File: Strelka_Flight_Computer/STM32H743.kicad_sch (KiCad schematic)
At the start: 40 parts, among them J3 Conn_01x07, Q3 AO3400A, Q4 AO3400A, Q5 AO3401A, SW2 TS-1185-C-A-A-A, SW3 TS-1185-C-A-A-A, U6 STM32H743VITx, Y1 Q13FC1350000400, Y2 X1E0000210834

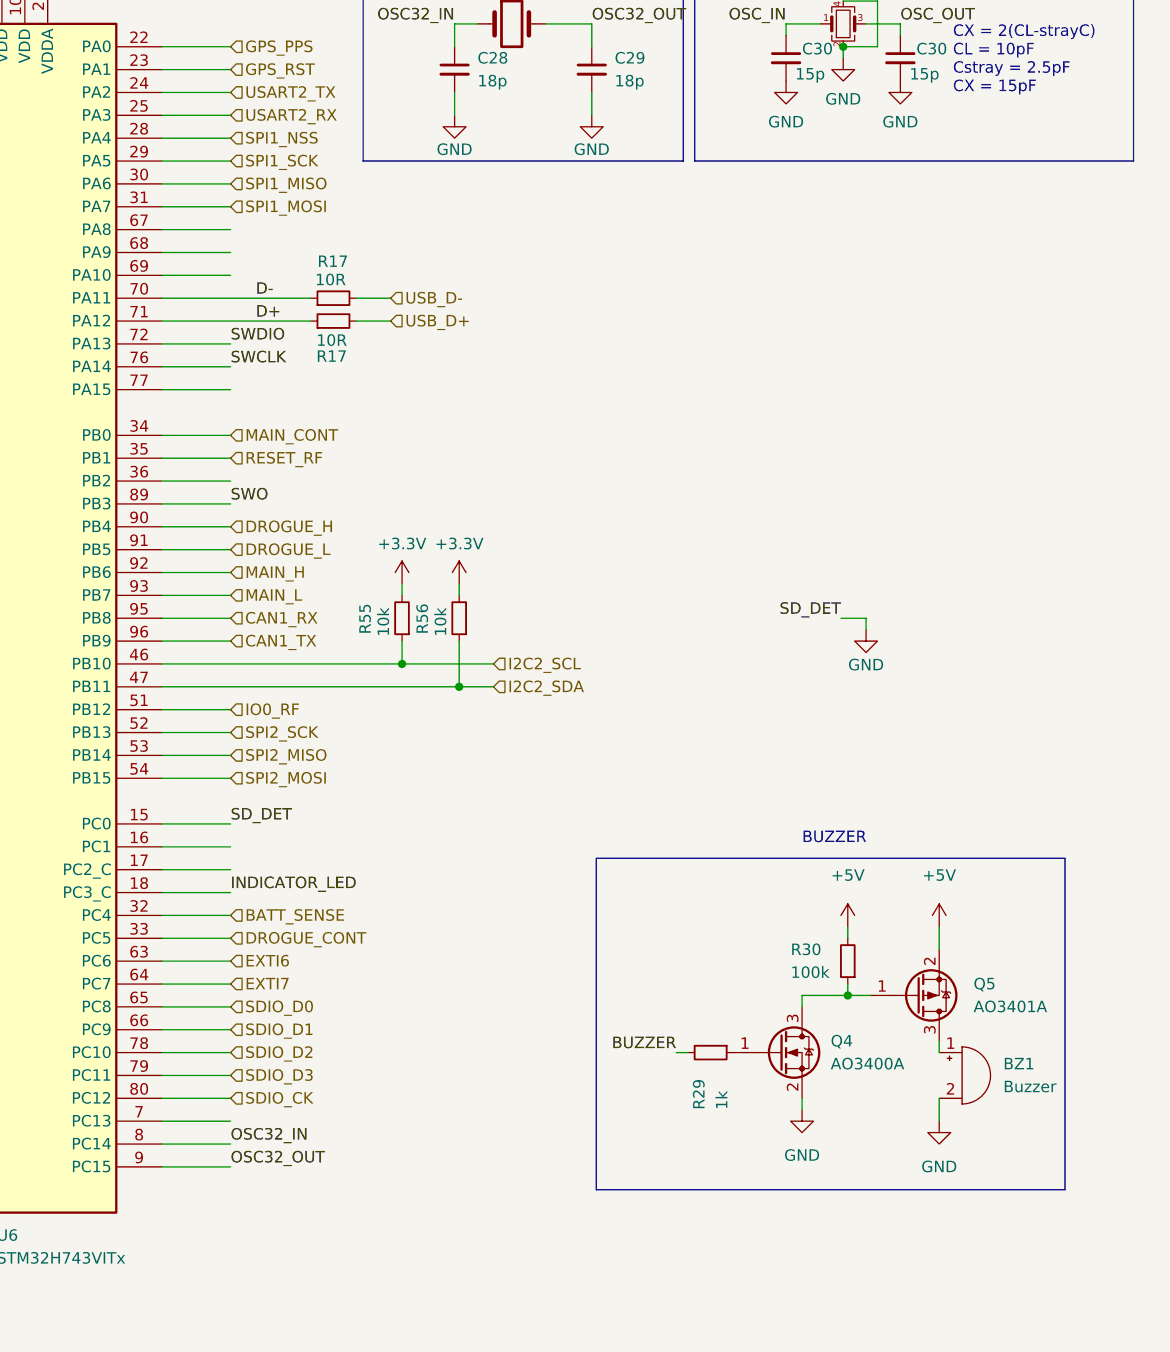
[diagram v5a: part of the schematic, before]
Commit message: Added lp filter caps to adc signals
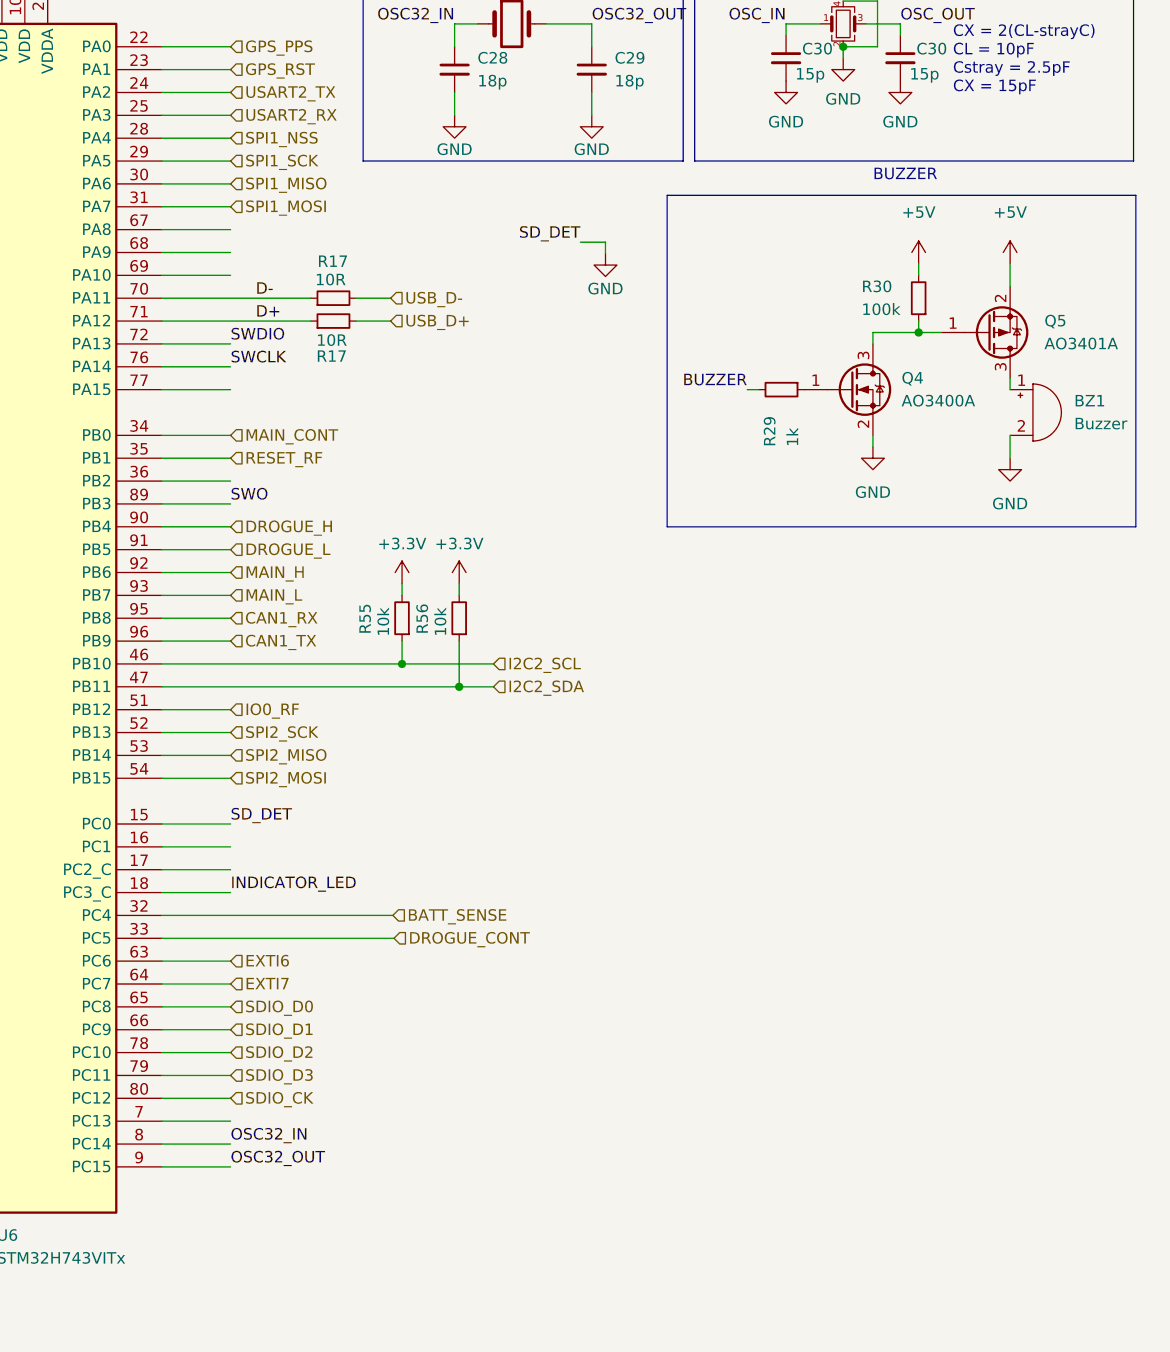
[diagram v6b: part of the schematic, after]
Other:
- moved on the sheet: BZ1, Q4, Q5, R29, R30

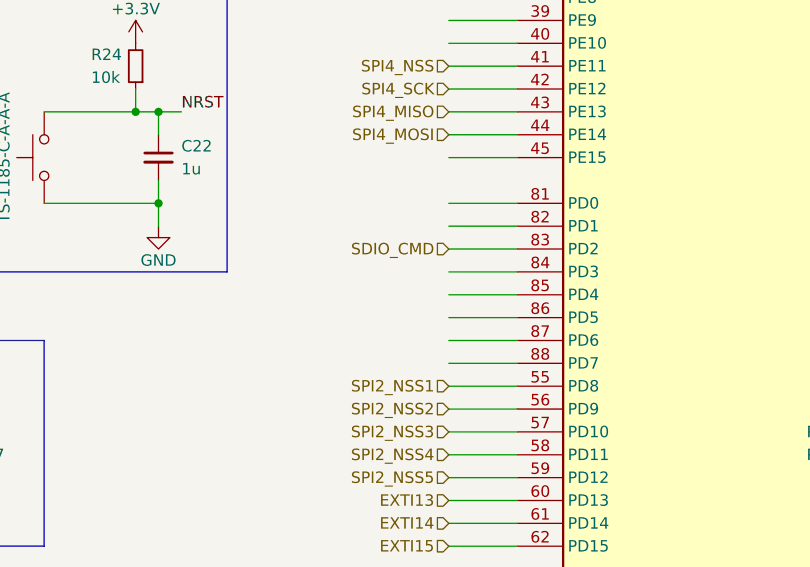
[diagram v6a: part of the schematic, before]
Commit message: Added LCSC mpn to all relevent parts
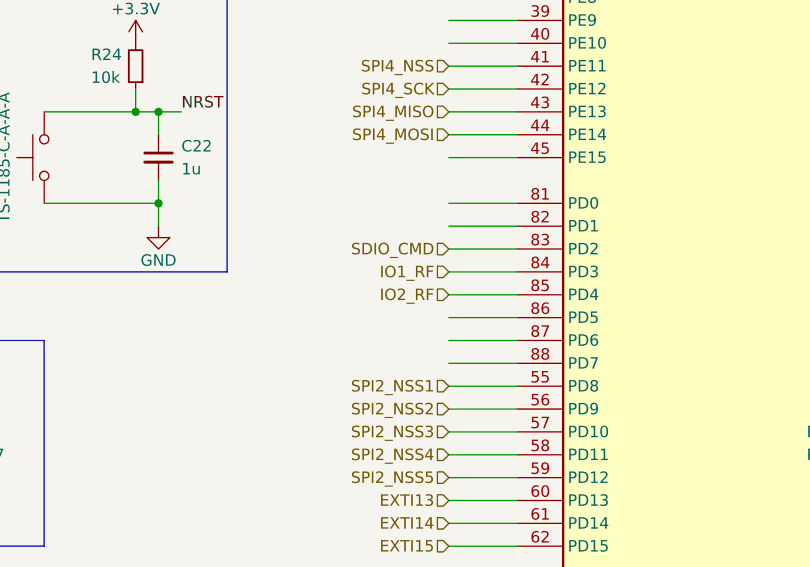
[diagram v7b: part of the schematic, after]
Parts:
- C13, C14, C15, C16, C17, C18, C21: LCSC (none) -> C1525
- C19, C20: LCSC (none) -> C12530
- C22: LCSC (none) -> C52923
- R19, R22, R23, R29: LCSC (none) -> C11702
- R20, R24, R55, R56: LCSC (none) -> C25744
- R21: LCSC C23140 -> C25105
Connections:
- net IO1_RF: now reaches U6.84 (PD3)
- net IO2_RF: now reaches U6.85 (PD4)
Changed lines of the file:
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@@
     (effects (font (size 1.27 1.27)) (justify left))
+  )
+  (hierarchical_label "IO1_RF" (shape input) (at 124.46 106.172 180) (fields_autoplaced)
+    (effects (font (size 1.27 1.27)) (justify right))
   )
   (hierarchical_label "SPI1_MOSI" (shape input) (at 182.88 50.292 0) (fields_autoplaced)
@@
     (effects (font (size 1.27 1.27)) (justify left))
   )
+  (hierarchical_label "IO2_RF" (shape input) (at 124.46 108.712 180) (fields_autoplaced)
+    (effects (font (size 1.27 1.27)) (justify right))
+  )
   (hierarchical_label "SPI2_SCK" (shape input) (at 182.88 108.712 0) (fields_autoplaced)
     (effects (font (size 1.27 1.27)) (justify left))
@@
       (effects (font (size 1.27 1.27)) hide)
     )
+    (property "LCSC" " C1525" (at 65.532 34.29 0)
+      (effects (font (size 1.27 1.27)) hide)
+    )
     (pin "1")
     (pin "2")
@@
       (effects (font (size 1.27 1.27)) hide)
     )
+    (property "LCSC" "C25744" (at 56.642 96.012 0)
+      (effects (font (size 1.27 1.27)) hide)
+    )
     (pin "1")
     (pin "2")
@@
       (effects (font (size 1.27 1.27)) hide)
     )
+    (property "LCSC" " C12530" (at 123.19 148.082 0)
+      (effects (font (size 1.27 1.27)) hide)
+    )
     (pin "1")
     (pin "2")
@@
       (effects (font (size 1.27 1.27)) hide)
     )
-    (property "LCSC" "C23140" (at 56.642 164.592 0)
+    (property "LCSC" "C25105" (at 56.642 164.592 0)
       (effects (font (size 1.27 1.27)) hide)
     )
@@
       (effects (font (size 1.27 1.27)) hide)
     )
+    (property "LCSC" "C25744" (at 208.28 96.012 90)
+      (effects (font (size 1.27 1.27)) hide)
+    )
     (pin "1")
     (pin "2")
@@
       (effects (font (size 1.27 1.27)) hide)
     )
+    (property "LCSC" " C11702" (at 83.312 164.592 0)
+      (effects (font (size 1.27 1.27)) hide)
+    )
     (pin "1")
     (pin "2")
@@
       (effects (font (size 1.27 1.27)) hide)
     )
+    (property "LCSC" " C11702" (at 70.612 164.592 0)
+      (effects (font (size 1.27 1.27)) hide)
+    )
     (pin "1")
     (pin "2")
@@
       (effects (font (size 1.27 1.27)) hide)
     )
+    (property "LCSC" " C1525" (at 55.372 34.29 0)
+      (effects (font (size 1.27 1.27)) hide)
+    )
     (pin "1")
     (pin "2")
@@
       (effects (font (size 1.27 1.27)) hide)
     )
+    (property "LCSC" " C1525" (at 92.202 34.29 0)
+      (effects (font (size 1.27 1.27)) hide)
+    )
     (pin "1")
     (pin "2")
@@
     )
     (property "Datasheet" "~" (at 201.93 96.012 0)
+      (effects (font (size 1.27 1.27)) hide)
+    )
+    (property "LCSC" "C25744" (at 201.93 96.012 90)
       (effects (font (size 1.27 1.27)) hide)
     )
@@
       (effects (font (size 1.27 1.27)) hide)
     )
+    (property "LCSC" " C1525" (at 171.45 19.812 0)
+      (effects (font (size 1.27 1.27)) hide)
+    )
     (pin "1")
     (pin "2")
@@
       (effects (font (size 1.27 1.27)) hide)
     )
+    (property "LCSC" " C1525" (at 74.422 34.29 0)
+      (effects (font (size 1.27 1.27)) hide)
+    )
     (pin "1")
     (pin "2")
@@
       (effects (font (size 1.27 1.27)) hide)
     )
+    (property "LCSC" " C1525" (at 45.212 34.29 0)
+      (effects (font (size 1.27 1.27)) hide)
+    )
     (pin "1")
     (pin "2")
@@
       (effects (font (size 1.27 1.27)) hide)
     )
+    (property "LCSC" " C1525" (at 83.312 34.29 0)
+      (effects (font (size 1.27 1.27)) hide)
+    )
     (pin "1")
     (pin "2")
@@
       (effects (font (size 1.27 1.27)) hide)
     )
+    (property "LCSC" "C25744" (at 89.662 83.312 0)
+      (effects (font (size 1.27 1.27)) hide)
+    )
     (pin "1")
     (pin "2")
@@
       (effects (font (size 1.27 1.27)) hide)
     )
+    (property "LCSC" " C52923" (at 92.202 93.472 0)
+      (effects (font (size 1.27 1.27)) hide)
+    )
     (pin "1")
     (pin "2")
@@
     )
     (property "Datasheet" "~" (at 114.3 145.542 0)
+      (effects (font (size 1.27 1.27)) hide)
+    )
+    (property "LCSC" " C12530" (at 114.3 145.542 0)
       (effects (font (size 1.27 1.27)) hide)
     )
@@
     )
     (property "Datasheet" "~" (at 244.094 70.612 0)
+      (effects (font (size 1.27 1.27)) hide)
+    )
+    (property "LCSC" " C11702" (at 244.094 70.612 0)
       (effects (font (size 1.27 1.27)) hide)
     )
@@
       (effects (font (size 1.27 1.27)) hide)
     )
+    (property "LCSC" " C11702" (at 43.942 173.482 0)
+      (effects (font (size 1.27 1.27)) hide)
+    )

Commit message: Adjusted changes after jlc tech team review
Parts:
- C30: LCSC C1644 -> C1548
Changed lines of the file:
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@@
       (effects (font (size 1.27 1.27)) hide)
     )
-    (property "LCSC" "C1644" (at 257.302 33.782 0)
+    (property "LCSC" "C1548" (at 257.302 33.782 0)
       (effects (font (size 1.27 1.27)) hide)
     )
@@
       (effects (font (size 1.27 1.27)) hide)
     )
-    (property "LCSC" "C1644" (at 244.602 33.782 0)
-      (effects (font (size 1.27 1.27)) hide)
-    )
+    (property "LCSC" "C1548" (at 244.602 33.782 0)
+      (effects (font (size 1.27 1.27)) hide)
+    )
